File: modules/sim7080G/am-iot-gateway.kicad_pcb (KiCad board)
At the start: 4 copper layers, 22 x 42 mm, 42 parts, among them J1 Bus_M.2_Socket_E, J3 GNSS Antenna, J4 RF Antenna, J5 NSIM-5-B, Q1 SS8050, Q2 SS8050, Q3 SS8050, U2 SIM7080G, U3 TXB0108RGY

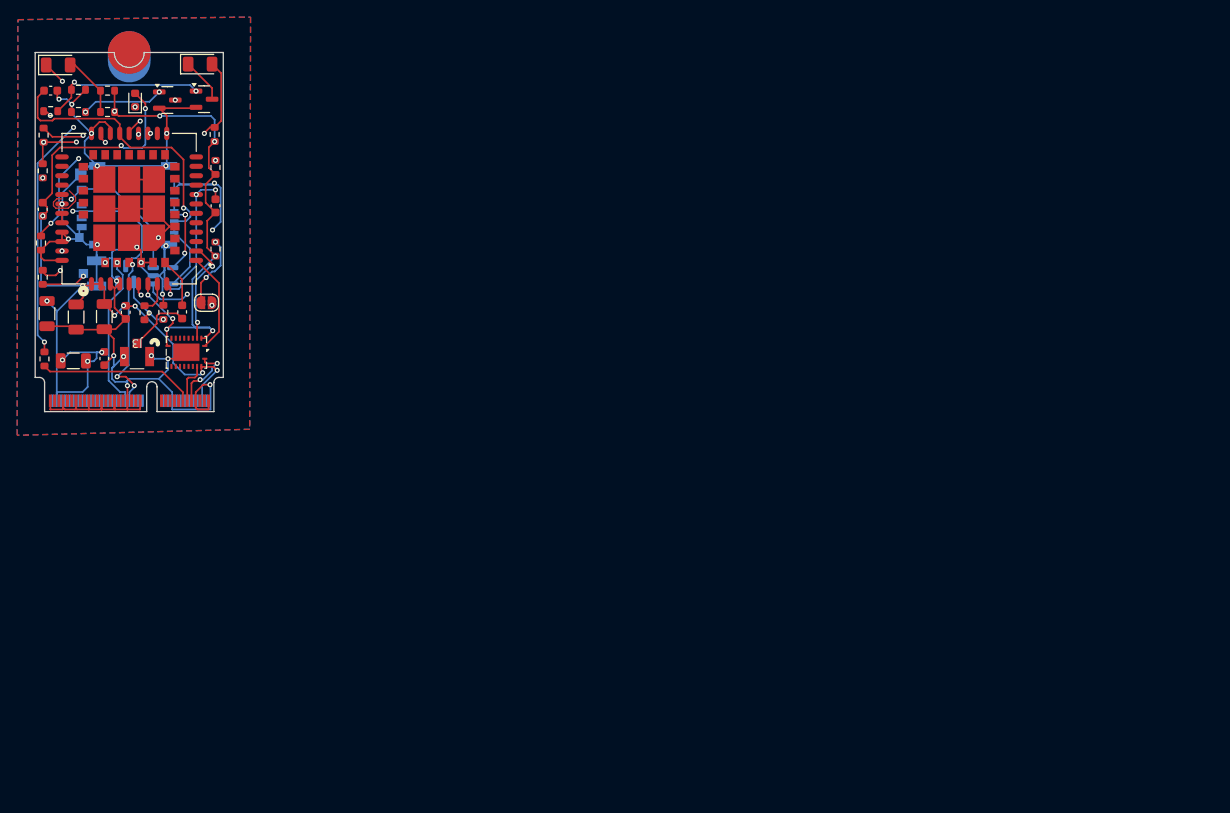
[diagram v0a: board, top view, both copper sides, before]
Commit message: fix: remodify board to be a baseboard
Signed-off-by: Rodney Osodo <socials@rodneyosodo.com>
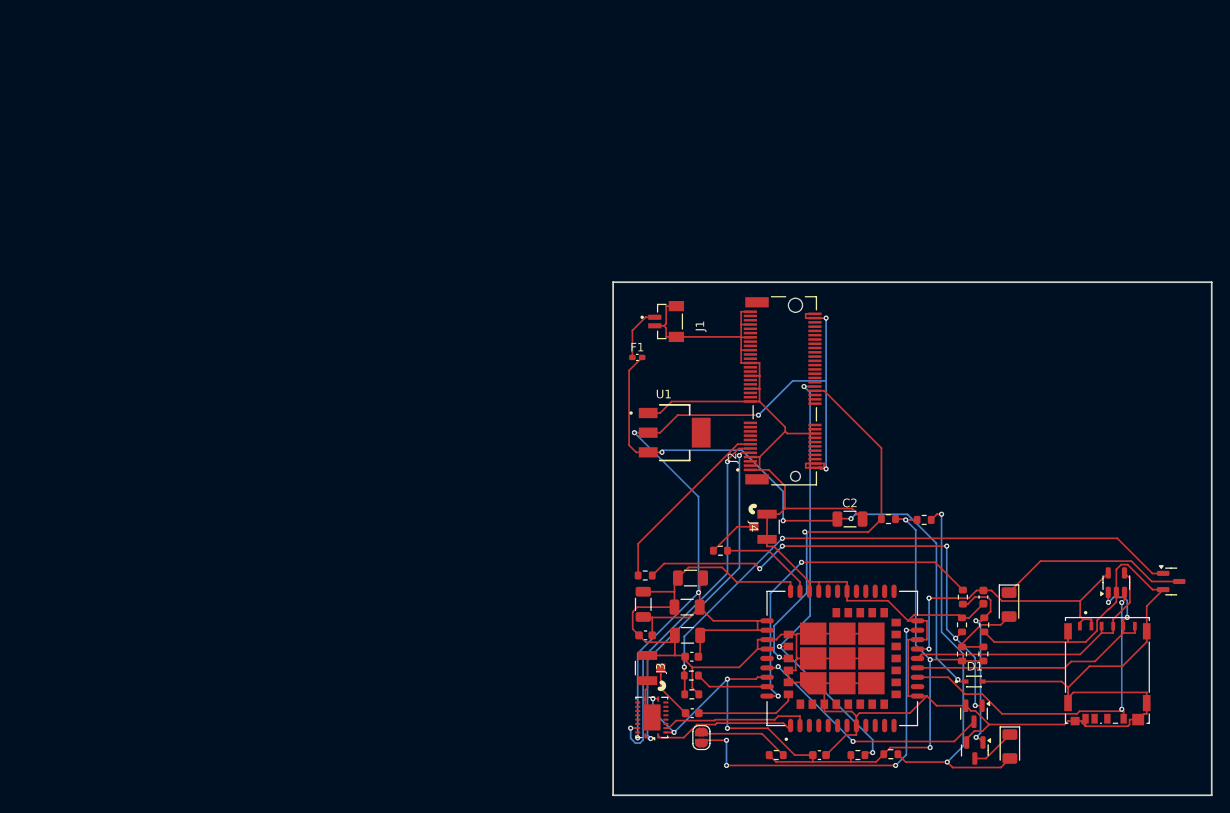
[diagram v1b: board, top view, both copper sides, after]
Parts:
- removed R1: 100, Resistor_SMD:R_0603_1608Metric
- added F1: Fuse, Fuse:Fuse_0402_1005Metric_Pad0.77x0.64mm_HandSolder, F.Cu at (152.6, 85.2)
- added J2: MDT420E03002, MDT420E03002:AMPHENOL_MDT420E03002, F.Cu at (171.1, 89.1)
- added U1: AZ1117IH-3.3TRG1, AZ1117IH-3.3TRG1:SOT230P700X185-4N, F.Cu at (157.0, 94.0)
- C1: value 100uF -> 10uF
- C2: value 1uF -> 10uF; footprint Capacitor_SMD:C_0603_1608Metric -> Capacitor_SMD:C_1206_3216Metric
- D1: value LED -> BZT52C12S; footprint LED_SMD:LED_0603_1608Metric -> BZT52C12S:DIO_BZT52C12S
- D3, J5, Q1: moved to F.Cu
- J1: value Bus_M.2_Socket_E -> BM02B-SRSS-TB_LF__SN_; footprint M.2-Key-E-Footprints-master:2242-key-E -> BM02B-SRSS-TB_LF__SN_:JST_BM02B-SRSS-TB_LF__SN_
- J3: footprint CONUFL001_SMD_T:CONN1_CONUFL_TEC -> CONUFL001:CONN1_CONUFL_TEC
- J4: footprint CONUFL001_SMD_T:CONN1_CONUFL_TEC -> CONUFL001:CONN1_CONUFL_TEC; moved to F.Cu
- moved D2 127.9 mm to (196.1, 114.1), turned to -90 degrees
- moved Q1 127.4 mm to (215.1, 111.4), turned to 0 degrees
- moved J5 126.6 mm to (207.6, 121.8), turned to 180 degrees
- moved C12 124.1 mm to (193.1, 113.2), turned to -90 degrees
- moved D4 123.8 mm to (196.2, 130.7), turned to -90 degrees
- moved R14 123.0 mm to (193.2, 116.5), turned to 90 degrees
- moved R4 121.8 mm to (193.1, 119.9), turned to 90 degrees
- moved R13 120.9 mm to (190.7, 113.2), turned to 90 degrees
- moved R16 119.5 mm to (190.6, 116.5), turned to -90 degrees
- moved D1 119.4 mm to (192.0, 123.1), turned to 0 degrees
- moved Q3 118.5 mm to (192.0, 126.9), turned to -90 degrees
- moved R3 118.3 mm to (190.6, 119.9), turned to 90 degrees
- moved Q2 118.0 mm to (192.1, 131.2), turned to -90 degrees
- moved D3 117.1 mm to (208.7, 111.5), turned to 90 degrees
- moved R12 112.4 mm to (186.2, 104.2), turned to 0 degrees
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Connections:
- C1 pad 2: +3V3 -> GND
- C2 pad 1: +3V3 -> Net-(U1-INPUT)
- C2 pad 2: +3V3 -> GND
- J1 pad 1: GND -> +9V
- J1 pad 2: +3V3 -> GND
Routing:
- net GND: track 218.1 -> 369.7 mm, vias 24 -> 0
- net Net-(U1-INPUT): track 0.00 -> 72.5 mm, vias 0 -> 4
- net Net-(Q1-B): track 7.36 -> 69.3 mm
- net SIM7080G_RXD: track 4.93 -> 43.9 mm, vias 0 -> 2
- net SIM7080G_TXD: track 8.10 -> 39.9 mm
- net +3V3: track 103.2 -> 127.7 mm, vias 13 -> 6
- net +1V8: track 73.1 -> 95.2 mm, vias 10 -> 7
- net Net-(D1-K): track 20.0 -> 0.00 mm, vias 3 -> 0
- net Net-(Q3-B): track 40.3 -> 58.2 mm, vias 4 -> 5
- net Net-(D4-A): track 29.6 -> 46.5 mm
- net Net-(JP1-B): track 30.1 -> 43.4 mm, vias 2 -> 4
- net Net-(D2-K): track 33.0 -> 22.4 mm, vias 2 -> 0
- net SIM7080G_SDA: track 42.3 -> 52.5 mm, vias 2 -> 3
- net PWR_KEY: track 39.0 -> 28.8 mm
- net SIM_CLK: track 44.2 -> 35.8 mm, vias 4 -> 2
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- removed copper zone on In2.Cu, net +1V8
- removed copper zone on In1.Cu, net +3V3
- removed copper zone on B.Cu, net GND
- removed copper zone on F.Cu, net GND
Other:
- board size 22 x 42 mm -> 70 x 60 mm
- copper layers 4 -> 2
